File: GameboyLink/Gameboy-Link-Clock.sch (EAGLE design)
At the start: 47 parts, among them IC1 MEGA8-P, J1 AVR_SPI_PRG_6PTH, Q1 16MHz, T1 EBC pinout

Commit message: GBClock board schematics drafted ok.
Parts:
- removed C5: 0.1uF, resistor:C-EU025-024X044
- removed CLK4543_POW, CLK4543_RAW: M01PTH, SparkFun-Connectors:M01PTH
- removed D1: germanium, diode:DIODE-D-7.5
- removed J_USBC: (no value), SparkFun-Connectors:USB_C_2-LAYER_PADS
- removed J_USBC_CC: (no value), SparkFun-Connectors:CONN_02PAD
- removed R1: 10k, resistor:R-EU_0204/5
- removed R2: (no value), resistor:R-EU_0204/5
- removed T1: EBC pinout, transistor:-NPN-TO92-EBC
- removed U$3: RTC4543-SA, kalshagar:RTC4543-SA
- added J_GB_CLASSIC: GB_LINK_CONNECTOR, kalshagar:GB_LINK_CONNECTOR
- added U1: DS1307Z, SparkFun-Clocks:DS1307Z
- added Y1: 32.768kHz, SparkFun-Clocks:CRYSTAL-32.768KHZPTH-2X6
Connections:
- removed net N$16: J_USBC.CC2, J_USBC_CC.2
- removed net N$17: J_USBC.CC1, J_USBC_CC.1
- removed net N$37: IC1.PC2(ADC2), U$3.CE
- removed net N$38: IC1.PC3(ADC3), U$3.WR
- removed net N$39: CLK4543_RAW.1, R1.2, U$3.FOUT
- removed net N$40: R1.1, T1.B
- removed net N$41: R2.1, T1.C
- removed net N$42: CLK4543_POW.1, R2.2
- new net N$23: U1.X1, Y1.2
- new net N$24: U1.X2, Y1.1
- net BATP: now also U1.VBATT; no longer D1.A
- net GB_CLK: now also J_GB_CLASSIC.GB_CLK
- net GB_MISO: now also J_GB_CLASSIC.GB_MISO
- net GB_MOSI: now also J_GB_CLASSIC.GB_MOSI
- net GB_SD: now also J_GB_CLASSIC.GB_SD
- net GB_VCC: now also J_GB_CLASSIC.GB_VCC
- net GND: now also J_GB_CLASSIC.GB_GND, U1.GND; no longer C5.1, J_USBC.GND, J_USBC.SHLD, T1.E, U$3.GND
- net N$1: now also U1.SCL; no longer U$3.CLOCK
- net N$2: now also U1.SDA; no longer U$3.DATA
- net USBD+: no longer J_USBC.D+
- net USBD-: no longer J_USBC.D-
- net USB_VCC: no longer J_USBC.VBUS
- net VCC: now also U1.VCC; no longer C5.2, D1.C, U$3.FOE, U$3.FSEL, U$3.VCC
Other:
- note removed: "High makes FOUT 1Hz (low=32kHz)"
- moved on the sheet: H1, H2, H3, H4

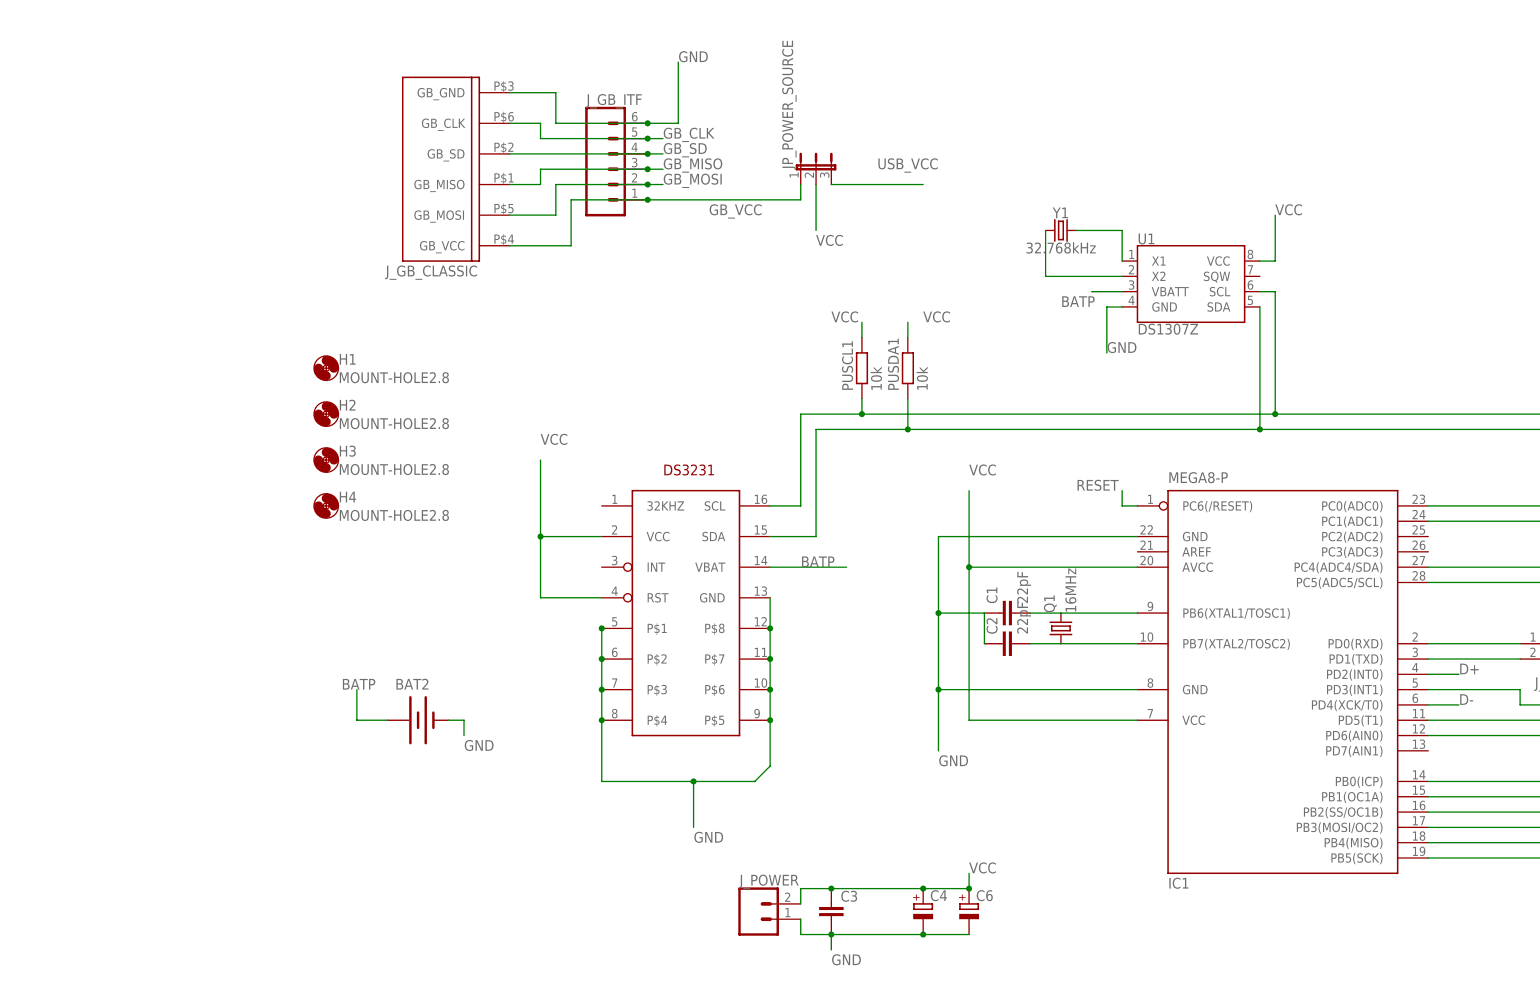
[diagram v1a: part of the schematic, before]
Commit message: Started the physical board of the GB Clock
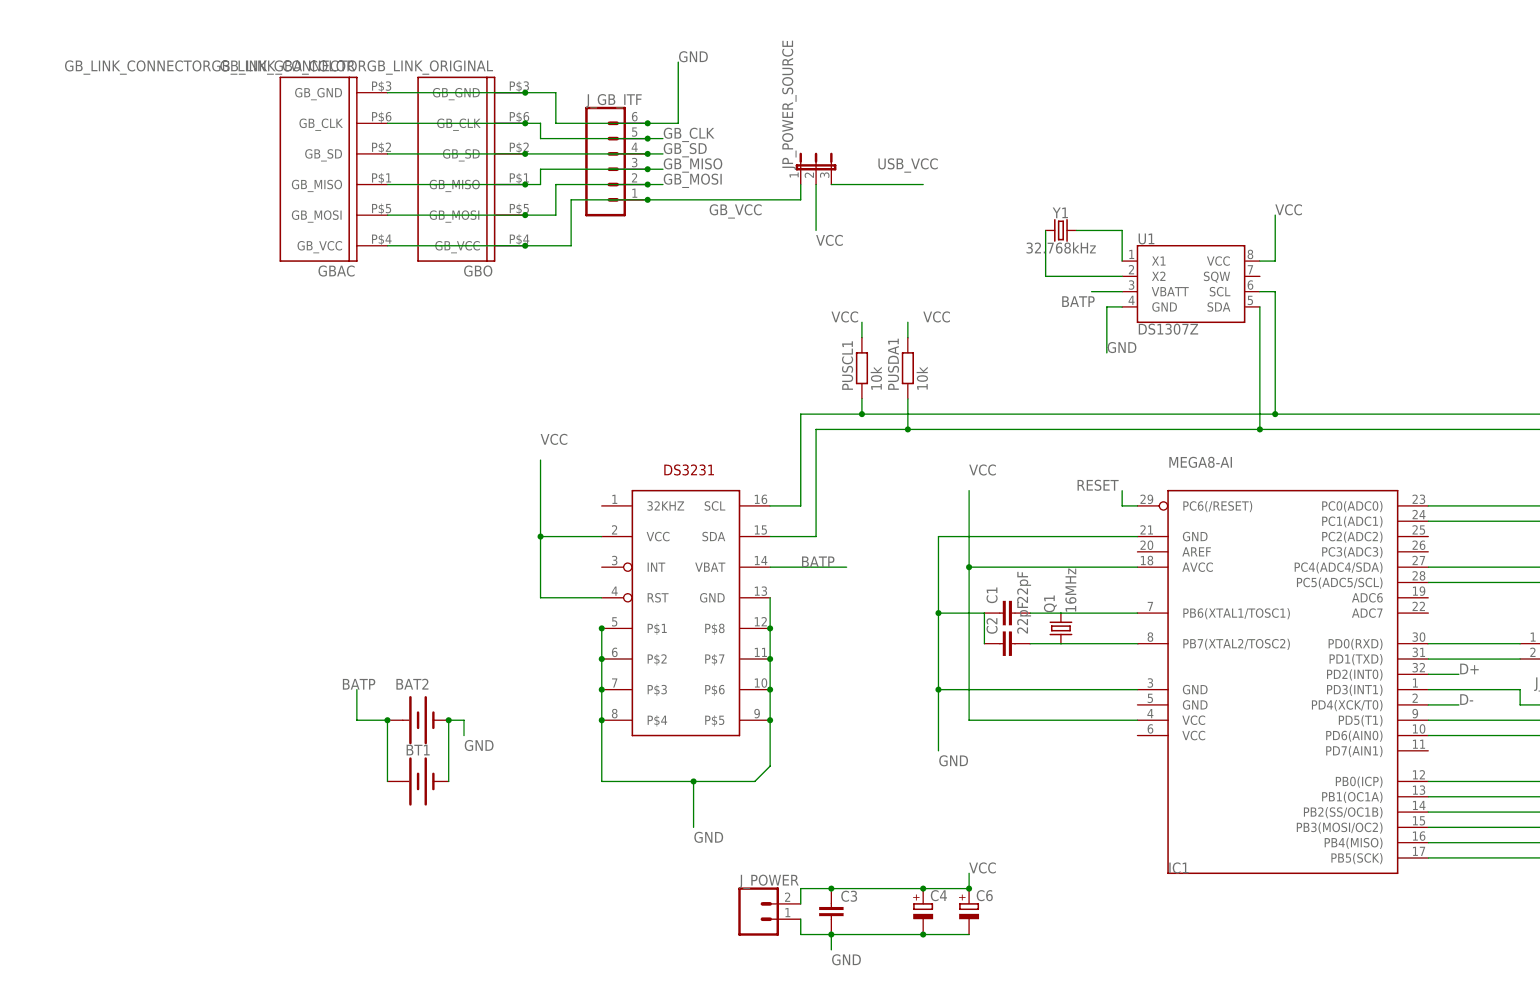
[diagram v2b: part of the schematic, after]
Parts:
- removed H1, H2, H3, H4: MOUNT-HOLE2.8, holes:MOUNT-HOLE2.8
- removed J_GB_CLASSIC: GB_LINK_CONNECTOR, kalshagar:GB_LINK_CONNECTOR
- added BT1: (no value), SparkFun-Batteries:BATTERY-20MM_SMD
- added GBAC: GB_LINK_CONNECTORGB_LINK_GBA_COLOR, kalshagar:GB_LINK_CONNECTORGB_LINK_GBA_COLOR
- added GBO: GB_LINK_CONNECTORGB_LINK_ORIGINAL, kalshagar:GB_LINK_CONNECTORGB_LINK_ORIGINAL
- BAT2: device SparkFun:BATTERY20PTH -> SparkFun-Batteries:BATTERY-20MM_PTH
- IC1: value MEGA8-P -> MEGA8-AI; device atmel:MEGA8-P -> atmel:MEGA8-AI
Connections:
- net BATP: now also BT1.+
- net GB_CLK: now also GBAC.GB_CLK, GBO.GB_CLK; no longer J_GB_CLASSIC.GB_CLK
- net GB_MISO: now also GBAC.GB_MISO, GBO.GB_MISO; no longer J_GB_CLASSIC.GB_MISO
- net GB_MOSI: now also GBAC.GB_MOSI, GBO.GB_MOSI; no longer J_GB_CLASSIC.GB_MOSI
- net GB_SD: now also GBAC.GB_SD, GBO.GB_SD; no longer J_GB_CLASSIC.GB_SD
- net GB_VCC: now also GBAC.GB_VCC, GBO.GB_VCC; no longer J_GB_CLASSIC.GB_VCC
- net GND: now also BT1.-, GBAC.GB_GND, GBO.GB_GND; no longer J_GB_CLASSIC.GB_GND
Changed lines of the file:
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@@
 <part name="JP_POWER_SOURCE" library="jumper" library_urn="urn:adsk.eagle:library:252" deviceset="JP2E" device="" package3d_urn="urn:adsk.eagle:package:15452/1"/>
 <part name="J_GB_ITF" library="SparkFun-Connectors" deviceset="CONN_06" device="NO_SILK_NO_POP"/>
-<part name="IC1" library="atmel" deviceset="MEGA8-P" device=""/>
+<part name="IC1" library="atmel" library_urn="urn:adsk.eagle:library:105" deviceset="MEGA8" device="-AI" package3d_urn="urn:adsk.eagle:package:4313/2"/>
 <part name="U$2" library="kalshagar" deviceset="DS3231" device="DS3231-SO16W"/>
 <part name="PUSCL1" library="resistor" deviceset="R-EU_" device="0204/5" value="10k"/>
@@
 <part name="DS1" library="SparkFun" deviceset="DS3234" device=""/>
 <part name="J1" library="SparkFun" deviceset="AVR_SPI_PRG_6" device="PTH"/>
-<part name="BAT2" library="SparkFun" deviceset="BATTERY" device="20PTH"/>
-<part name="H1" library="holes" deviceset="MOUNT-HOLE" device="2.8"/>
-<part name="H2" library="holes" deviceset="MOUNT-HOLE" device="2.8"/>
-<part name="H3" library="holes" deviceset="MOUNT-HOLE" device="2.8"/>
-<part name="H4" library="holes" deviceset="MOUNT-HOLE" device="2.8"/>
+<part name="BAT2" library="SparkFun-Batteries" deviceset="BATTERY" device="-20MM_PTH"/>
 <part name="USB_MINI" library="SparkFun-Connectors" deviceset="USB" device="SMD"/>
 <part name="USB_MICRO" library="SparkFun-Connectors" deviceset="USB_MICROB_PLUG" device="CONN-11752"/>
@@
 <part name="D2" library="SparkFun-LED" deviceset="LED" device="1206"/>
 <part name="D3" library="SparkFun-LED" deviceset="LED" device="1206"/>
-<part name="J_GB_CLASSIC" library="kalshagar" deviceset="GB_LINK_CONNECTOR" device=""/>
 <part name="U1" library="SparkFun-Clocks" deviceset="DS1307" device="Z"/>
 <part name="Y1" library="SparkFun-Clocks" deviceset="CRYSTAL-32.768KHZ" device="PTH-2X6" value="32.768kHz"/>
+<part name="GBAC" library="kalshagar" deviceset="GB_LINK_CONNECTOR" device="GB_LINK_GBA_COLOR"/>
+<part name="GBO" library="kalshagar" deviceset="GB_LINK_CONNECTOR" device="GB_LINK_ORIGINAL"/>
+<part name="BT1" library="SparkFun-Batteries" deviceset="BATTERY" device="-20MM_SMD"/>
 </parts>
 <sheets>
@@
 <attribute name="NAME" x="60.96" y="-35.052" size="1.778" layer="95" font="vector"/>
 </instance>
-<instance part="IC1" gate="G$1" x="175.26" y="-129.54" smashed="yes">
-<attribute name="NAME" x="157.48" y="-165.1" size="1.778" layer="95"/>
-<attribute name="VALUE" x="157.48" y="-97.79" size="1.778" layer="96"/>
+<instance part="IC1" gate="G$1" x="175.26" y="-127" smashed="yes">
+<attribute name="NAME" x="157.48" y="-162.56" size="1.778" layer="95"/>
+<attribute name="VALUE" x="157.48" y="-95.25" size="1.778" layer="96"/>
 </instance>
 <instance part="U$2" gate="G$1" x="81.28" y="-109.22" smashed="yes"/>
@@
 <attribute name="VALUE" x="29.21" y="-143.51" size="1.778" layer="96"/>
 </instance>
-<instance part="H1" gate="G$1" x="17.78" y="-78.74" smashed="yes">
-<attribute name="NAME" x="19.812" y="-78.1558" size="1.778" layer="95"/>
-<attribute name="VALUE" x="19.812" y="-81.2038" size="1.778" layer="96"/>
-</instance>
-<instance part="H2" gate="G$1" x="17.78" y="-86.36" smashed="yes">
-<attribute name="NAME" x="19.812" y="-85.7758" size="1.778" layer="95"/>
-<attribute name="VALUE" x="19.812" y="-88.8238" size="1.778" layer="96"/>
-</instance>
-<instance part="H3" gate="G$1" x="17.78" y="-93.98" smashed="yes">
-<attribute name="NAME" x="19.812" y="-93.3958" size="1.778" layer="95"/>
-<attribute name="VALUE" x="19.812" y="-96.4438" size="1.778" layer="96"/>
-</instance>
-<instance part="H4" gate="G$1" x="17.78" y="-101.6" smashed="yes">
-<attribute name="NAME" x="19.812" y="-101.0158" size="1.778" layer="95"/>
-<attribute name="VALUE" x="19.812" y="-104.0638" size="1.778" layer="96"/>
-</instance>
 <instance part="USB_MINI" gate="G$1" x="355.6" y="-71.12" smashed="yes"/>
 <instance part="USB_MICRO" gate="G$1" x="358.14" y="-48.26" smashed="yes">
@@
 <attribute name="VALUE" x="291.592" y="-120.015" size="1.778" layer="96" font="vector" rot="R180" align="top-left"/>
 </instance>
-<instance part="J_GB_CLASSIC" gate="G$1" x="40.64" y="-45.72" smashed="yes" rot="R180">
-<attribute name="NAME" x="42.926" y="-61.722" size="1.778" layer="95" rot="R180"/>
-</instance>
 <instance part="U1" gate="G$1" x="160.02" y="-63.5" smashed="yes">
 <attribute name="NAME" x="152.4" y="-58.166" size="1.778" layer="95" font="vector"/>
@@
 <attribute name="NAME" x="139.7" y="-53.848" size="1.778" layer="95" font="vector" align="bottom-center"/>
 <attribute name="VALUE" x="139.7" y="-57.912" size="1.778" layer="96" font="vector" align="top-center"/>
+</instance>
+<instance part="GBAC" gate="G$1" x="20.32" y="-45.72" smashed="yes" rot="R180">
+<attribute name="NAME" x="22.606" y="-61.722" size="1.778" layer="95" rot="R180"/>
+<attribute name="VALUE" x="22.606" y="-27.686" size="1.778" layer="96" rot="R180"/>
+</instance>
+<instance part="GBO" gate="G$1" x="43.18" y="-45.72" smashed="yes" rot="R180">
+<attribute name="NAME" x="45.466" y="-61.722" size="1.778" layer="95" rot="R180"/>
+<attribute name="VALUE" x="45.466" y="-27.686" size="1.778" layer="96" rot="R180"/>
+</instance>
+<instance part="BT1" gate="G$1" x="33.02" y="-147.32" smashed="yes">
+<attribute name="NAME" x="33.02" y="-143.002" size="1.778" layer="95" font="vector" align="bottom-center"/>
+<attribute name="VALUE" x="33.02" y="-151.638" size="1.778" layer="96" font="vector" align="top-center"/>
 </instance>
 </instances>
@@
 <wire x1="40.64" y1="-137.16" x2="40.64" y2="-139.7" width="0.1524" layer="91"/>
 <label x="40.64" y="-142.24" size="1.778" layer="95"/>
+<pinref part="BT1" gate="G$1" pin="-"/>
+<wire x1="38.1" y1="-147.32" x2="38.1" y2="-137.16" width="0.1524" layer="91"/>
+<junction x="38.1" y="-137.16"/>
 </segment>
 <segment>
@@
 <wire x1="55.88" y1="-38.1" x2="55.88" y2="-33.02" width="0.1524" layer="91"/>
 <junction x="71.12" y="-38.1"/>
-<wire x1="55.88" y1="-33.02" x2="48.26" y2="-33.02" width="0.1524" layer="91"/>
-<pinref part="J_GB_CLASSIC" gate="G$1" pin="GB_GND"/>
+<wire x1="55.88" y1="-33.02" x2="50.8" y2="-33.02" width="0.1524" layer="91"/>
+<pinref part="GBO" gate="G$1" pin="GB_GND"/>
+<pinref part="GBAC" gate="G$1" pin="GB_GND"/>
+<wire x1="50.8" y1="-33.02" x2="27.94" y2="-33.02" width="0.1524" layer="91"/>
+<junction x="50.8" y="-33.02"/>
 </segment>
 <segment>
@@
 <wire x1="22.86" y1="-137.16" x2="22.86" y2="-132.08" width="0.1524" layer="91"/>
 <label x="20.32" y="-132.08" size="1.778" layer="95"/>
+<pinref part="BT1" gate="G$1" pin="+"/>
+<wire x1="27.94" y1="-137.16" x2="27.94" y2="-147.32" width="0.1524" layer="91"/>
+<junction x="27.94" y="-137.16"/>
 </segment>
 <segment>
@@
 <junction x="71.12" y="-50.8"/>
 <wire x1="58.42" y1="-50.8" x2="58.42" y2="-58.42" width="0.1524" layer="91"/>
-<wire x1="58.42" y1="-58.42" x2="48.26" y2="-58.42" width="0.1524" layer="91"/>
-<pinref part="J_GB_CLASSIC" gate="G$1" pin="GB_VCC"/>
+<wire x1="58.42" y1="-58.42" x2="50.8" y2="-58.42" width="0.1524" layer="91"/>
+<pinref part="GBO" gate="G$1" pin="GB_VCC"/>
+<pinref part="GBAC" gate="G$1" pin="GB_VCC"/>
+<wire x1="27.94" y1="-58.42" x2="50.8" y2="-58.42" width="0.1524" layer="91"/>
+<junction x="50.8" y="-58.42"/>
 </segment>
 </net>
@@
 <junction x="71.12" y="-40.64"/>
 <wire x1="53.34" y1="-40.64" x2="53.34" y2="-38.1" width="0.1524" layer="91"/>
-<wire x1="53.34" y1="-38.1" x2="48.26" y2="-38.1" width="0.1524" layer="91"/>
-<pinref part="J_GB_CLASSIC" gate="G$1" pin="GB_CLK"/>
+<wire x1="53.34" y1="-38.1" x2="50.8" y2="-38.1" width="0.1524" layer="91"/>
+<pinref part="GBO" gate="G$1" pin="GB_CLK"/>
+<pinref part="GBAC" gate="G$1" pin="GB_CLK"/>
+<wire x1="27.94" y1="-38.1" x2="50.8" y2="-38.1" width="0.1524" layer="91"/>
+<junction x="50.8" y="-38.1"/>
 </segment>
 </net>
@@
 <wire x1="71.12" y1="-43.18" x2="73.66" y2="-43.18" width="0.1524" layer="91"/>
 <label x="73.66" y="-43.18" size="1.778" layer="95"/>
-<wire x1="71.12" y1="-43.18" x2="48.26" y2="-43.18" width="0.1524" layer="91"/>
+<wire x1="71.12" y1="-43.18" x2="50.8" y2="-43.18" width="0.1524" layer="91"/>
 <junction x="71.12" y="-43.18"/>
-<pinref part="J_GB_CLASSIC" gate="G$1" pin="GB_SD"/>
+<pinref part="GBO" gate="G$1" pin="GB_SD"/>
+<pinref part="GBAC" gate="G$1" pin="GB_SD"/>
+<wire x1="50.8" y1="-43.18" x2="27.94" y2="-43.18" width="0.1524" layer="91"/>
+<junction x="50.8" y="-43.18"/>
 </segment>
 </net>
@@
 <junction x="71.12" y="-45.72"/>
 <wire x1="53.34" y1="-45.72" x2="53.34" y2="-48.26" width="0.1524" layer="91"/>
-<wire x1="53.34" y1="-48.26" x2="48.26" y2="-48.26" width="0.1524" layer="91"/>
-<pinref part="J_GB_CLASSIC" gate="G$1" pin="GB_MISO"/>
+<wire x1="53.34" y1="-48.26" x2="50.8" y2="-48.26" width="0.1524" layer="91"/>
+<pinref part="GBO" gate="G$1" pin="GB_MISO"/>
+<pinref part="GBAC" gate="G$1" pin="GB_MISO"/>
+<wire x1="27.94" y1="-48.26" x2="50.8" y2="-48.26" width="0.1524" layer="91"/>
+<junction x="50.8" y="-48.26"/>
 </segment>
 </net>
@@
 <junction x="71.12" y="-48.26"/>
 <wire x1="55.88" y1="-48.26" x2="55.88" y2="-53.34" width="0.1524" layer="91"/>
-<wire x1="55.88" y1="-53.34" x2="48.26" y2="-53.34" width="0.1524" layer="91"/>
-<pinref part="J_GB_CLASSIC" gate="G$1" pin="GB_MOSI"/>
-</segment>
-</net>
+<wire x1="55.88" y1="-53.34" x2="50.8" y2="-53.34" width="0.1524" layer="91"/>
+<pinref part="GBO" gate="G$1" pin="GB_MOSI"/>
+<pinref part="GBAC" gate="G$1" pin="GB_MOSI"/>
+<wire x1="27.94" y1="-53.34" x2="50.8" y2="-53.34" width="0.1524" layer="91"/>
+<junction x="50.8" y="-53.34"/>
+</segment>
+</net>

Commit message: All components on the board, now routing and adjustments.
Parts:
- PUSCL1, PUSDA1: device resistor:R-EU_0204/5 -> rcl:R-EU_0207/2V
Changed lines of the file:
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@@
 <part name="IC1" library="atmel" library_urn="urn:adsk.eagle:library:105" deviceset="MEGA8" device="-AI" package3d_urn="urn:adsk.eagle:package:4313/2"/>
 <part name="U$2" library="kalshagar" deviceset="DS3231" device="DS3231-SO16W"/>
-<part name="PUSCL1" library="resistor" deviceset="R-EU_" device="0204/5" value="10k"/>
-<part name="PUSDA1" library="resistor" deviceset="R-EU_" device="0204/5" value="10k"/>
+<part name="PUSCL1" library="rcl" library_urn="urn:adsk.eagle:library:334" deviceset="R-EU_" device="0207/2V" package3d_urn="urn:adsk.eagle:package:23490/1" value="10k"/>
+<part name="PUSDA1" library="rcl" library_urn="urn:adsk.eagle:library:334" deviceset="R-EU_" device="0207/2V" package3d_urn="urn:adsk.eagle:package:23490/1" value="10k"/>
 <part name="Q1" library="crystal" deviceset="CRYSTAL" device="HC49S" value="16MHz"/>
 <part name="C1" library="resistor" deviceset="C-EU" device="025-024X044" value="22pF"/>

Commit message: Before manual routing
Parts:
- removed DS1: DS3234, SparkFun:DS3234
- removed JP_D+, JP_D-: TEST-POINT3X5, SparkFun-Passives:TEST-POINT3X5
- removed J_GB_ITF: (no value), SparkFun-Connectors:CONN_06NO_SILK_NO_POP
- added J_GB_DBG: FEMALE 2x3, SparkFun-Connectors:CONN_03X2FEMALE
- added R1, R2: 10k, rcl:R-EU_R1206
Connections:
- removed net N$9: DS1.CS, IC1.PB2(SS/OC1B)
- net BATP: no longer DS1.VBAT
- net D+: no longer JP_D+.1
- net D-: no longer JP_D-.1
- net GB_CLK: now also J_GB_DBG.5; no longer J_GB_ITF.5
- net GB_MISO: now also J_GB_DBG.3; no longer J_GB_ITF.3
- net GB_MOSI: now also J_GB_DBG.2; no longer J_GB_ITF.2
- net GB_SD: now also J_GB_DBG.4; no longer J_GB_ITF.4
- net GB_VCC: now also J_GB_DBG.1; no longer J_GB_ITF.1
- net GND: now also J_GB_DBG.6; no longer DS1.GND, DS1.GND@10, DS1.GND@11, DS1.GND@12, DS1.GND@13, DS1.GND@14, DS1.GND@2, DS1.GND@7, DS1.GND@8, DS1.GND@9, J_GB_ITF.6
- net N$1: now also R2.1
- net N$2: now also R1.1
- net N$3: no longer DS1.SCLK@18, DS1.SCLK@20
- net N$7: no longer DS1.DIN
- net N$8: no longer DS1.DOUT
- net RESET: no longer DS1.RST
- net VCC: now also R1.2, R2.2; no longer DS1.VCC
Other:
- moved on the sheet: JP_POWER_SOURCE
